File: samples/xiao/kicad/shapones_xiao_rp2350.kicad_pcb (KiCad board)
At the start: 2 copper layers, 100 x 50 mm, 74 parts, among them J1 JST S2B-PH-SM4-TB, J3 Micro_SD_Card_Det_Hirose_DM3AT, J4 Hong Cheng HC-PM254-5.0H-2x10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, J5 Conn_01x01, J6 Conn_01x01, Q1 IRLML6344TRPBF, Q2 IRLML6344TRPBF, Q3 IRLML2246TRPBF, Q4 IRLML2246TRPBF, SW1 GT-TC018A-H0375-L1, SW10 GT-TC018A-H0375-L1, SW2 Rubber, SW3 Rubber, SW4 Rubber, SW5 Rubber, SW6 Rubber, SW7 Rubber, SW8 Rubber, SW9 Rubber, U1 XIAO RP2350, U2 RT9080-33GJ5, U3 74VHC1G126, U4 HT82V73A, U5 PCA9555PW, U6 M154-240240-RGB

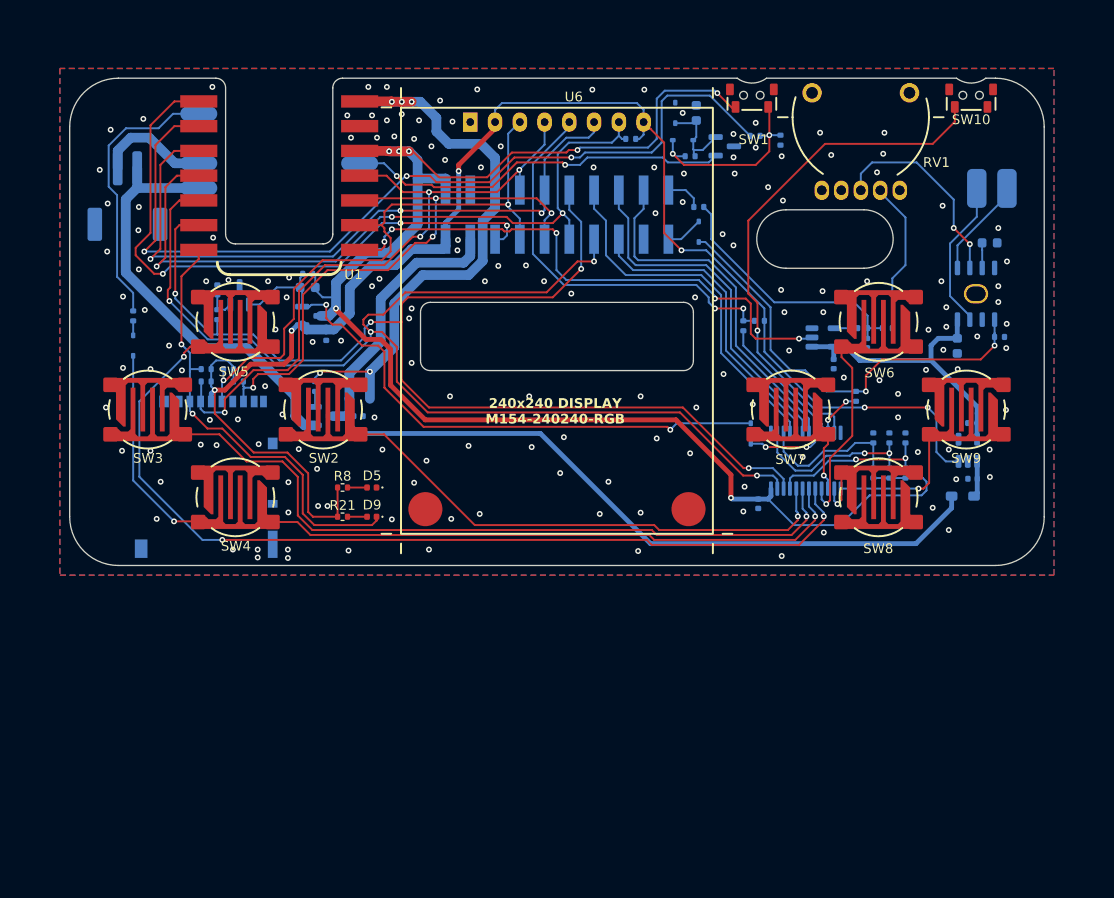
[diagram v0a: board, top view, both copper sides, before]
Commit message: add tooling strips
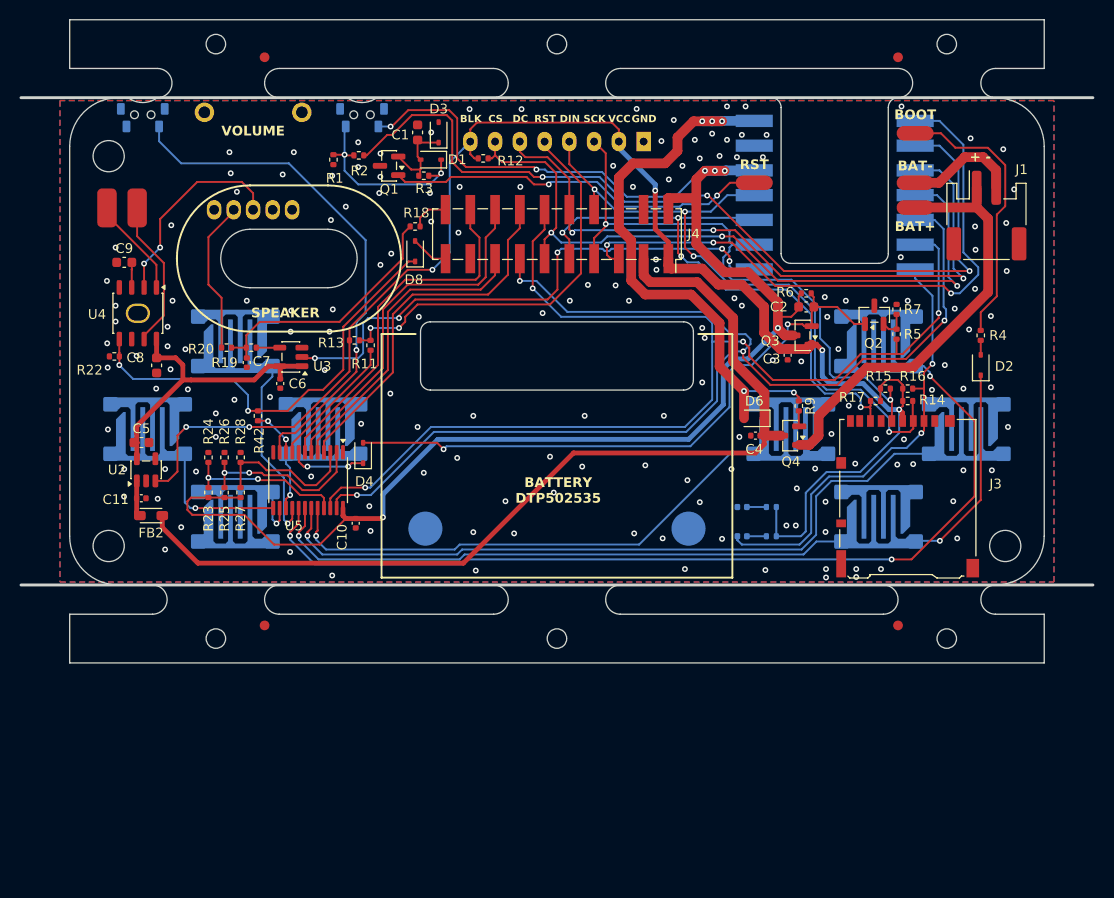
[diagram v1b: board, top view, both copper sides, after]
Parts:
- added FID1: Fiducial, Fiducial:Fiducial_1mm_Mask2mm, F.Cu at (135.0, 45.9)
- added FID2: Fiducial, Fiducial:Fiducial_1mm_Mask2mm, F.Cu at (70.0, 45.9)
- added FID3: Fiducial, Fiducial:Fiducial_1mm_Mask2mm, F.Cu at (135.0, 104.2)
- added FID4: Fiducial, Fiducial:Fiducial_1mm_Mask2mm, F.Cu at (70.0, 104.2)
- C1, C10, C11, C2, C3, C4, C6, C7, C8, C9, D1, D2, D3, D4, D6, D8, FB2, J1, J3, J4, J5, J6, Q1, Q2, Q3, Q4, R1, R11, R12, R13, R14, R15, R16, R17, R18, R19, R2, R20, R22, R23, R24, R25, R26, R27, R28, R3, R4, R42, R5, R6, R7, R9, U2, U3, U4, U5: moved to F.Cu
- C5: footprint Capacitor_SMD:C_0402_1005Metric -> Capacitor_SMD:C_0603_1608Metric; moved to F.Cu
- D5, D9, R21, R8, RV1, SW1, SW10, SW2, SW3, SW4, SW5, SW6, SW7, SW8, SW9, U1, U6: moved to B.Cu
- moved J6 92.4 mm to (53.8, 61.3), turned to 0 degrees
- moved R22 90.8 mm to (54.6, 76.5), turned to 180 degrees
- moved C9 88.8 mm to (55.6, 66.9), turned to 0 degrees
- moved J1 88.2 mm to (144.1, 62.1), turned to 0 degrees
- moved D2 87.0 mm to (143.5, 77.4)
- moved R4 87.0 mm to (143.5, 74.4)
- moved J5 86.2 mm to (56.9, 61.3), turned to 0 degrees
- moved U4 86.0 mm to (57.0, 72.1)
- moved C11 85.3 mm to (57.4, 91.1), turned to 0 degrees
- moved C5 85.3 mm to (57.4, 85.4), turned to 0 degrees
- moved SW10 85.0 mm to (57.5, 51.8), turned to 180 degrees
- moved U2 84.3 mm to (57.8, 88.2)
- moved SW3 84.0 mm to (142.0, 84.0), turned to 0 degrees
- moved SW9 84.0 mm to (58.0, 84.0), turned to 0 degrees
- moved FB2 83.3 mm to (58.4, 92.9), turned to 180 degrees
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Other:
- board size 100 x 50 mm -> 110 x 66 mm
- board text added: "V-CUT"

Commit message: Orders made to JLCPCB
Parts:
- removed FID1, FID2, FID3, FID4: Fiducial, Fiducial:Fiducial_1mm_Mask2mm
- removed J5, J6: Conn_01x01, Connector_Wire:SolderWirePad_1x01_SMD_2x4mm
- added J2: Conn_01x02, shpc_mechanical:SolderWirePad_1x02_SMD_150x50mil, F.Cu at (55.4, 62.2)
- FB2: footprint Inductor_SMD:L_Walsin_WLFM201209x -> Inductor_SMD:L_0805_2012Metric
- moved D5 52.9 mm to (85.0, 51.6)
- moved R8 52.1 mm to (89.2, 51.6)
- moved R18 21.3 mm to (67.8, 75.2), turned to -90 degrees
- moved C7 2.66 mm to (66.4, 75.2), turned to 90 degrees
- moved R3 2.49 mm to (84.1, 59.1)
- moved J1 2.45 mm to (144.1, 64.5)
- moved R1 2.41 mm to (76.7, 54.0), turned to 180 degrees
- moved D1 2.29 mm to (85.0, 57.3)
- moved R4 2.19 mm to (143.5, 76.6)
- moved C6 2.14 mm to (69.8, 78.1)
- moved Q1 1.96 mm to (80.9, 57.5)
- moved R2 1.95 mm to (79.9, 54.0)
- moved D2 1.81 mm to (143.5, 79.2)
- moved R17 1.64 mm to (131.1, 80.9), turned to -90 degrees
- moved R20 1.33 mm to (64.8, 75.7)
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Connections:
- net Net-(U5-A0) renamed /IOEX_A0
- net Net-(U5-A1) renamed /IOEX_A1
- net Net-(U5-A2) renamed /IOEX_A2
- J4 pad 12: /I2C_SCL -> /I2C_SDA
- J4 pad 13: /I2C_SDA -> /I2C_SCL
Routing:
- net /EXT_AUDIO: track 3.85 -> 28.6 mm
- net Net-(C7-Pad1): track 26.8 -> 3.71 mm
- net /I2C_SCL: track 120.1 -> 114.1 mm
- net Net-(U6-RES): track 41.7 -> 35.9 mm, vias 2 -> 1
- net /SOUND: track 57.0 -> 62.3 mm
- net /LCD_CS: track 75.4 -> 80.2 mm
- net +3V3: track 163.0 -> 158.2 mm
- net /SW_DOWN: track 82.0 -> 77.8 mm
- net VPERI: track 158.9 -> 154.7 mm, vias 6 -> 4
- net /I2C_SDA: track 119.1 -> 122.6 mm
- net Net-(Q1-D): track 39.5 -> 43.0 mm
- net /XIAO_GPIO: track 63.5 -> 67.0 mm
- net /LCD_DC: track 69.8 -> 72.4 mm
- net Net-(U1-BOOT): track 28.6 -> 30.9 mm
- net Net-(U1-GP27): track 90.2 -> 92.2 mm
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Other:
- board size 110 x 66 mm -> 100 x 50 mm
- board text added: "+"
- board text added: "-"
- board text added: "0"
- board text added: "1"
- board text added: "A0"
- board text added: "A1"
- board text added: "A2"
- board text added: "BL"
- board text added: "FUNC"
- board text added: "POWER"
- board text added: "Rev.1"
- board text added: "XIAO"
- board text added: "Xiaonsole"
- board text added: "©Shapoco"
- board text removed: "BLK"
- board text removed: "V-CUT"

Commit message: fix
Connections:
- net /MUTE_INT renamed /INT_MUTE
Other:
- board text added: "Rev.2"
- board text added: "Shapoco"
- board text removed: "Rev.1"
- board text removed: "©Shapoco"
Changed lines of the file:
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@@
 	(net 44 "/IOEX1")
 	(net 45 "/IOEX3")
-	(net 46 "/MUTE_INT")
+	(net 46 "/INT_MUTE")
 	(net 47 "Net-(U4-IN)")
 	(net 48 "/SOUND")
@@
 			(layers "F.Cu" "F.Mask" "F.Paste")
 			(roundrect_rratio 0.25)
-			(net 46 "/MUTE_INT")
+			(net 46 "/INT_MUTE")
 			(pintype "passive")
 		)
@@
 			(layers "F.Cu" "F.Mask" "F.Paste")
 			(roundrect_rratio 0.25)
-			(net 46 "/MUTE_INT")
+			(net 46 "/INT_MUTE")
 			(pinfunction "IO0_6")
 			(pintype "bidirectional")
@@
 		(sheetname "/")
 		(sheetfile "shapones_xiao_rp2350.kicad_sch")
-		(attr smd dnp)
+		(attr smd)
 		(fp_line
 			(start -0.153641 0.38)
@@
 			)
 		)
-		(property "Datasheet" ""
+		(property "Datasheet" "~"
 			(at 0 0 180)
 			(unlocked yes)
@@
 			)
 		)
-		(property "Description" ""
+		(property "Description" "Push button switch, generic, two pins"
 			(at 0 0 180)
 			(unlocked yes)
@@
 			)
 		)
-		(property "Datasheet" ""
+		(property "Datasheet" "~"
 			(at 0 0 0)
 			(unlocked yes)
@@
 			)
 		)
-		(property "Description" ""
+		(property "Description" "Push button switch, generic, two pins"
 			(at 0 0 0)
 			(unlocked yes)
@@
 			)
 		)
-		(property "Datasheet" ""
+		(property "Datasheet" "~"
 			(at 0 0 180)
 			(unlocked yes)
@@
 			)
 		)
-		(property "Description" ""
+		(property "Description" "Push button switch, generic, two pins"
 			(at 0 0 180)
 			(unlocked yes)
@@
 			)
 		)
-		(property "Datasheet" ""
+		(property "Datasheet" "~"
 			(at 0 0 180)
 			(unlocked yes)
@@
 			)
 		)
-		(property "Description" ""
+		(property "Description" "Push button switch, generic, two pins"
 			(at 0 0 180)
 			(unlocked yes)
@@
 			)
 		)
-		(property "Datasheet" ""
+		(property "Datasheet" "~"
 			(at 0 0 180)
 			(unlocked yes)
@@
 			)
 		)
-		(property "Description" ""
+		(property "Description" "Push button switch, generic, two pins"
 			(at 0 0 180)
 			(unlocked yes)
@@
 			)
 		)
-		(property "Datasheet" ""
+		(property "Datasheet" "~"
 			(at 0 0 180)
 			(unlocked yes)
@@
 			)
 		)
-		(property "Description" ""
+		(property "Description" "Push button switch, generic, two pins"
 			(at 0 0 180)
 			(unlocked yes)
@@
 			)
 		)
-		(property "Datasheet" ""
+		(property "Datasheet" "~"
 			(at 0 0 180)
 			(unlocked yes)
@@
 			)
 		)
-		(property "Description" ""
+		(property "Description" "Push button switch, generic, two pins"
 			(at 0 0 180)
 			(unlocked yes)
@@
 			)
 		)
-		(property "Datasheet" ""
+		(property "Datasheet" "~"
 			(at 0 0 180)
 			(unlocked yes)
@@
 			)
 		)
-		(property "Description" ""
+		(property "Description" "Push button switch, generic, two pins"
 			(at 0 0 180)
 			(unlocked yes)
@@
 		(layer "Edge.Cuts")
 	)
-	(gr_text "Rev.1"
+	(gr_text "Rev.2"
 		(at 58.547 57.404 0)
 		(layer "F.Mask")
@@
 		)
 	)
-	(gr_text "©Shapoco"
+	(gr_text "Shapoco"
 		(at 73.025 57.404 0)
 		(layer "F.Mask")

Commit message: fix
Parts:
- removed D4, D8: 1N4148WS, Diode_SMD:D_SOD-323
- removed R42: 10k, Resistor_SMD:R_0402_1005Metric
- added Q5: IRLML2246TRPBF, Package_TO_SOT_SMD:SOT-23, F.Cu at (70.7, 81.8)
- added R10: 100k, Resistor_SMD:R_0402_1005Metric, F.Cu at (73.4, 81.4)
- added R29: 10k, Resistor_SMD:R_0402_1005Metric, F.Cu at (79.4, 94.0)
- added R30: 10k, Resistor_SMD:R_0402_1005Metric, F.Cu at (80.5, 94.0)
- R5: value 10k -> 100k
- R7: value 100k -> 1M
- moved C10 3.18 mm to (80.0, 90.6), turned to -90 degrees
- moved D6 1.98 mm to (121.9, 81.8)
- moved C4 1.87 mm to (120.9, 83.4)
- moved R22 1.18 mm to (55.8, 76.7), turned to 0 degrees
- moved Q2 0.54 mm to (132.9, 72.7), turned to 0 degrees
- moved R5 0.51 mm to (135.5, 73.8)
- moved Q3 0.22 mm to (125.2, 74.2)
- moved R7 0.22 mm to (135.0, 71.5), turned to 180 degrees
- moved C3 0.19 mm to (123.7, 76.2)
- moved R9 0.13 mm to (124.2, 81.7)
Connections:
- Q2 pad 3: GND -> /PERI_EN_N
- R22 pad 2: GND -> VANL
- R7 pad 2: GND -> /PERI_EN_N
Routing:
- net /PERI_EN_N: track 7.93 -> 80.9 mm
- net Net-(Q2-D): track 62.9 -> 9.07 mm, vias 2 -> 0
- net Net-(Q5-S): track 43.5 -> 20.8 mm
- net /EXT_MUTE: track 3.88 -> 25.5 mm
- net /I2C_SDA: track 122.6 -> 126.8 mm
- net +3V3: track 158.2 -> 162.0 mm
- net /I2C_SCL: track 114.1 -> 117.2 mm
- net Net-(Q2-G): track 2.56 -> 5.49 mm
- net VANL: track 29.5 -> 32.1 mm
- net /EXT_AUDIO: track 28.6 -> 27.4 mm
- net /INT_MUTE: track 5.01 -> 6.05 mm
- net VPERI: track 154.7 -> 154.1 mm
- net /+BAT: track 45.1 -> 45.7 mm
- net GND: vias 199 -> 196

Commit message: fix
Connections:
- net /EXT_MUTE renamed /SPK_MUTE
- net /INT_MUTE renamed /IOEX_MUTE

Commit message: fix
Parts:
- removed R11: 0, Resistor_SMD:R_0402_1005Metric
- added D4: 1N4148WS, Diode_SMD:D_SOD-323, F.Cu at (72.6, 83.5)
- added D7: 1N4148WS, Diode_SMD:D_SOD-323, F.Cu at (80.5, 75.8)
- moved Q5 1.19 mm to (69.5, 81.8)
- moved R10 0.90 mm to (72.8, 80.8)
- moved R13 0.38 mm to (78.9, 75.9), turned to -90 degrees
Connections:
- Q5 pad 1: /IOEX_MUTE -> Net-(D4-A)
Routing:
- net /IOEX_MUTE: track 6.05 -> 2.05 mm, vias 2 -> 0
- net Net-(Q5-S): track 20.8 -> 18.3 mm
- net Net-(D4-A): track 0.00 -> 2.29 mm
- net Net-(D7-A): track 35.9 -> 36.6 mm
- net /SPK_MUTE: track 25.5 -> 26.2 mm
